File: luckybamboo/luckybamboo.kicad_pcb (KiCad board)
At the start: 4 copper layers, 70.7 x 53.3 mm, 148 parts, among them J1 NEIGHBOR1, J10 TEST_2P, J11 TEST_2P, J12 TEST_2P, J13 TEST_2P, J14 TEST_2P, J15 TEST_2P, J16 TEST_2P, J17 Conn_Coaxial, J18 Conn_Coaxial, J19 TEST_2P, J2 NEIGHBOR2, J20 TEST_2P, J21 TEST_2P, J22 TEST_2P, J23 TEST_2P, J24 TEST_2P, J25 TEST_2P, J26 TEST_2P, J27 TEST_2P, J28 TEST_2P, J29 TEST_2P, J3 Conn_01x08, J30 TEST_2P, J31 TEST_2P, J32 TEST_2P, J33 TEST_2P, J4 Conn_01x08, J5 Conn_01x08, J6 Conn_01x08, J7 BONUS_ROW, J8 TEST_2P, J9 TEST_2P, U1 ADF7242, U10 ADF7242_balun, U11 ADF7242_balun, U12 HHM2293A1, U13 BGA7H1N6, U14 ADF7242_balun, U15 ADF7242_balun, U16 ADF7242_balun, U17 ADF7242_balun, U2 ADF7242, U3 ADF7242, U4 ADF7242, U5 SKY13322, U6 HHM2293A1, U7 HHM2293A1, U8 ADF7242_balun, U9 ADF7242_balun, X1 XTAL4PIN, X2 XTAL4PIN, X3 XTAL4PIN, X4 XTAL4PIN

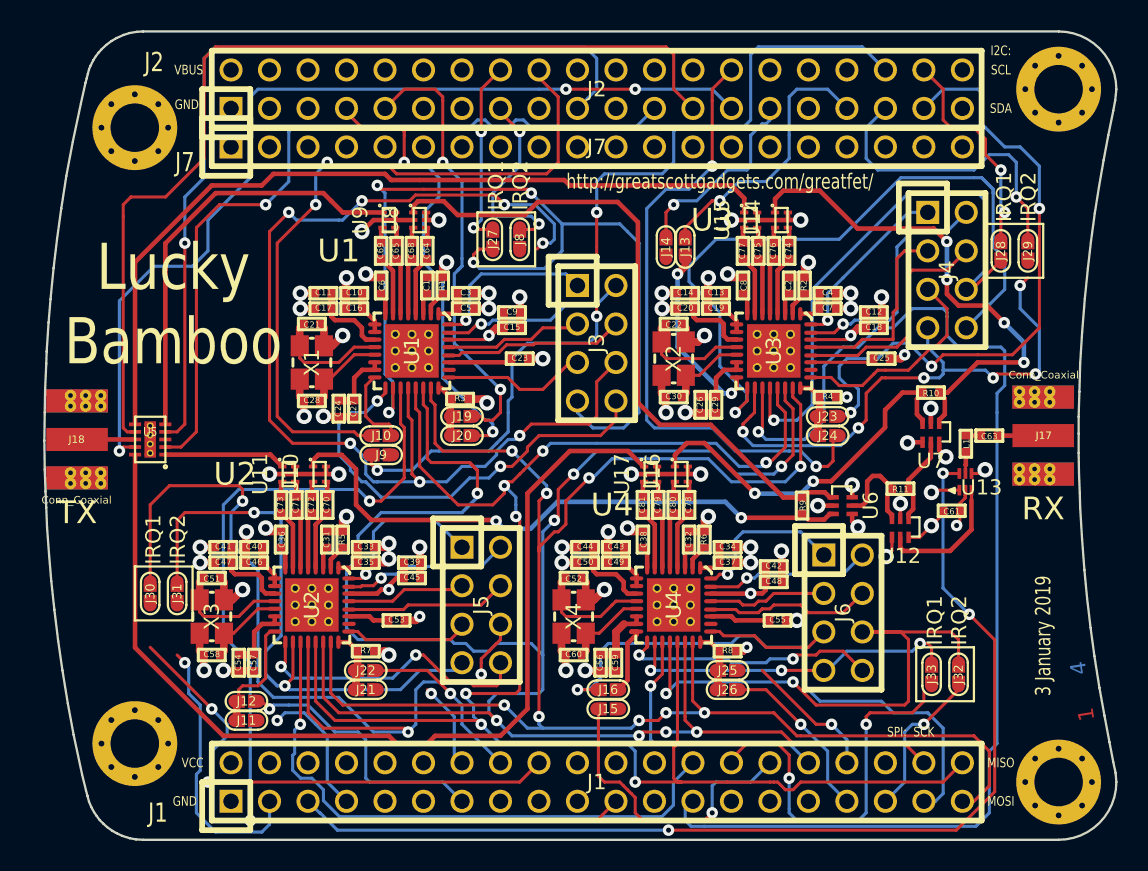
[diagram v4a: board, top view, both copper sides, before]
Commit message: Changed  Changed SPI CS 3 and IRQ1 3 pins, which were interfering with SPIFI. Added DC blocking capacitors near TX switch
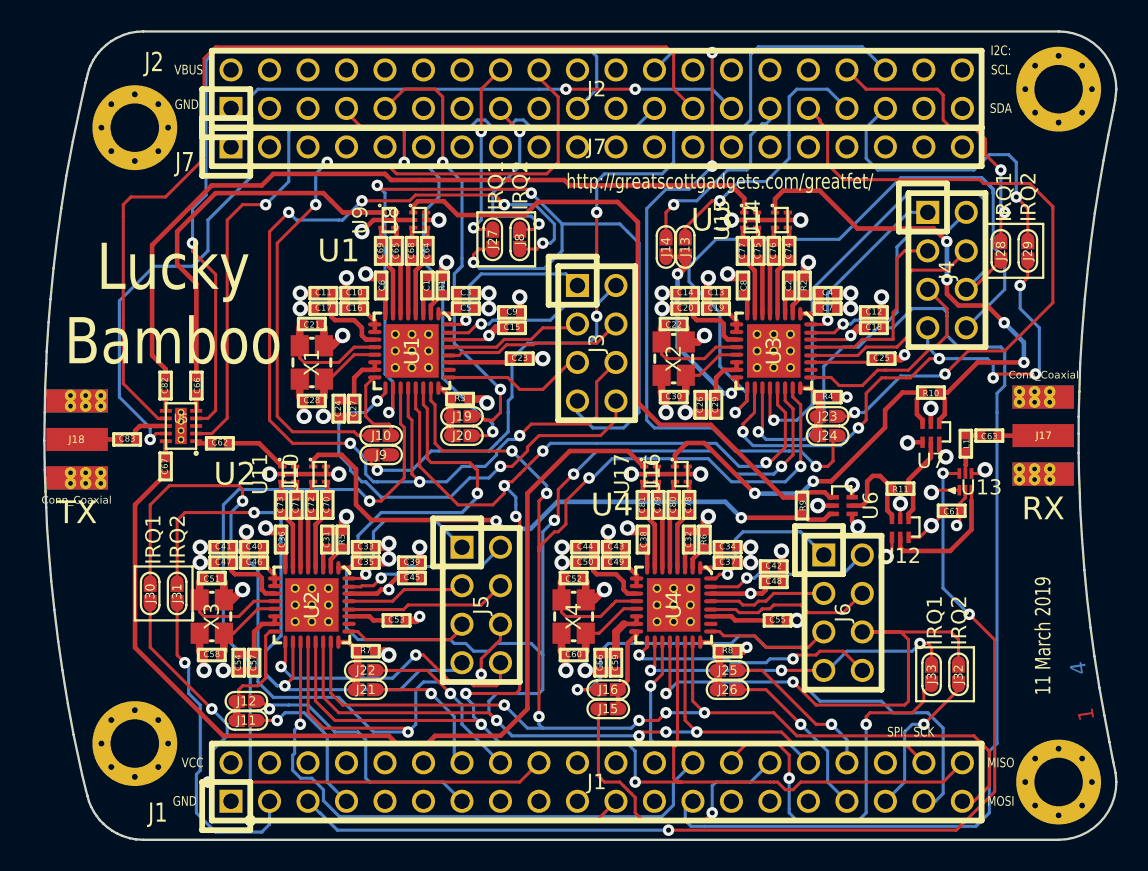
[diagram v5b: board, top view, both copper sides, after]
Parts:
- added C62: 47pF, gsg-modules:0402, F.Cu at (121.2, 95.8)
- added C66: 47pF, gsg-modules:0402, F.Cu at (119.6, 91.9)
- added C67: 47pF, gsg-modules:0402, F.Cu at (117.6, 97.3)
- added C82: 47pF, gsg-modules:0402, F.Cu at (117.6, 91.9)
- added C83: 47pF, gsg-modules:0402, F.Cu at (115.1, 95.5)
- moved U5 2.22 mm to (118.6, 94.6)
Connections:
- J1 pad 10: /P1_1 -> (no net)
- J1 pad 11: /CLK0 -> (no net)
- J1 pad 12: /P1_2 -> (no net)
- J1 pad 15: /P1_7 -> (no net)
- J1 pad 17: /P1_9 -> (no net)
- J1 pad 19: /P5_3 -> (no net)
- J1 pad 20: /P1_10 -> (no net)
- J1 pad 22: /P1_11 -> (no net)
- J1 pad 23: /P5_5 -> (no net)
- J1 pad 24: /P5_4 -> (no net)
- J1 pad 27: /P5_6 -> (no net)
- J1 pad 29: /P5_7 -> (no net)
- J1 pad 31: /P1_18 -> (no net)
- J1 pad 36: /P6_0 -> (no net)
- J1 pad 4: /P0_0 -> (no net)
- J1 pad 6: /P0_1 -> (no net)
- J1 pad 8: /P5_0 -> (no net)
- J1 pad 9: /P5_1 -> (no net)
- J18 pad 1: Net-(J18-Pad1) -> Net-(C83-Pad2)
- J2 pad 10: /P4_6 -> (no net)
- J2 pad 11: /P4_7 -> (no net)
- J2 pad 12: /CLK2 -> (no net)
- J2 pad 13: /P2_8 -> (no net)
- J2 pad 14: /P2_7 -> (no net)
- J2 pad 17: /WAKEUP0 -> (no net)
- J2 pad 2: Net-(J2-Pad2) -> (no net)
- J2 pad 20: /P2_3 -> (no net)
- J2 pad 21: /PF_4 -> (no net)
- J2 pad 22: /P3_2 -> (no net)
- J2 pad 26: /P3_0 -> (no net)
- J2 pad 28: /P3_4 -> (no net)
- J2 pad 3: /P4_8 -> (no net)
- J2 pad 30: /P3_7 -> (no net)
- J2 pad 32: /P3_3 -> (no net)
- J2 pad 37: /P3_5 -> (no net)
- J2 pad 38: /P3_6 -> (no net)
- J2 pad 39: /I2C0_SDA -> (no net)
- J2 pad 4: /P4_0 -> (no net)
- J2 pad 40: /I2C0_SCL -> (no net)
- J2 pad 5: /ADC0_0 -> (no net)
- J2 pad 6: /P4_5 -> (no net)
- J2 pad 8: /P4_2 -> (no net)
- J23 pad 2: /P3_5 -> /P6_7
- J24 pad 2: /P3_4 -> /P3_1
- J28 pad 1: /P3_6 -> /P6_6
- J7 pad 11: /RESET -> (no net)
- J7 pad 12: /VBAT -> (no net)
- J7 pad 13: /P2_11 -> (no net)
- J7 pad 14: /P2_10 -> (no net)
- J7 pad 15: /P6_10 -> (no net)
- J7 pad 16: /P6_9 -> (no net)
- J7 pad 17: /P6_2 -> (no net)
- J7 pad 18: /P6_1 -> (no net)
- J7 pad 2: /P6_4 -> (no net)
- J7 pad 3: /P6_5 -> (no net)
- J7 pad 4: /ADC0_5 -> (no net)
- J7 pad 5: /ADC0_2 -> (no net)
- J7 pad 6: /P2_9 -> (no net)
- J7 pad 7: /P2_12 -> (no net)
- J7 pad 8: /P2_13 -> (no net)
- J7 pad 9: /RTC_ALARM -> (no net)
- U1 pad 26: /RXEN1 -> (no net)
- U2 pad 26: /RXEN2 -> (no net)
- U3 pad 26: /RXEN3 -> (no net)
- U4 pad 26: /RXEN4 -> (no net)
- U5 pad 1: /RFOUT2 -> Net-(C62-Pad2)
- U5 pad 10: /RFOUT4 -> Net-(C67-Pad1)
- U5 pad 3: Net-(U5-Pad3) -> (no net)
- U5 pad 5: /RFOUT1 -> Net-(C66-Pad1)
- U5 pad 6: /RFOUT3 -> Net-(C82-Pad2)
- U5 pad 8: Net-(J18-Pad1) -> Net-(C83-Pad1)
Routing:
- net /P3_1: track 0.00 -> 46.7 mm, vias 0 -> 3
- net /P6_7: track 0.00 -> 43.9 mm, vias 0 -> 2
- net /P3_5: track 42.1 -> 0.00 mm, vias 3 -> 0
- net /P3_4: track 41.7 -> 0.00 mm, vias 2 -> 0
- net /P6_6: track 0.00 -> 19.4 mm, vias 0 -> 2
- net /P3_6: track 14.5 -> 0.00 mm, vias 2 -> 0
- net Net-(J18-Pad1): track 3.83 -> 0.00 mm
- net /RFOUT2: track 8.04 -> 4.22 mm
- net /P5_2: track 5.77 -> 9.19 mm
- net /P4_9: track 18.2 -> 21.7 mm
- net /RFOUT3: track 54.9 -> 51.7 mm
- net /P1_8: track 33.9 -> 36.8 mm
- net /RFOUT1: track 28.2 -> 25.3 mm
- net Net-(C83-Pad2): track 0.00 -> 2.77 mm
- net Net-(C83-Pad1): track 0.00 -> 2.73 mm
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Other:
- board text added: "11 March 2019"
- board text removed: "3 January 2019"
